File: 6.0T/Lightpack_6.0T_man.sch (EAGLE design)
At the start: 32 parts, among them IC1 AT90USB162, IC2 DM631_SOP24, IC3 DM631_SOP24, J1 DCJ0202, Q1 16Mhz, X1 USB-MICRO-B

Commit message: Front-line I/O rearranged
* Button --> DJK02A --> microUSB
* Expand PCB size for Alex case
* Bottom polygons shape changes
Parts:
- U$1: value RJ11-5P-REEL-LIGHTPACK6T -> RJ11-5P-REEL-LIGHTPACK6T2; device _RJ11:RJ11-5P-REEL-LIGHTPACK6T -> _RJ11:RJ11-5P-REEL-LIGHTPACK6T2
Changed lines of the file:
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@@
 <part name="SV1" library="_brd-conn" deviceset="UART3" device=""/>
 <part name="GND5" library="supply1" deviceset="GND" device=""/>
-<part name="U$1" library="_RJ11" deviceset="RJ11-5P-REEL" device="-LIGHTPACK6T"/>
+<part name="U$1" library="_RJ11" deviceset="RJ11-5P-REEL" device="-LIGHTPACK6T2"/>
 <part name="U$2" library="_RJ11" deviceset="RJ11-5P-REEL" device="-MAIN"/>
 <part name="J1" library="_connectors" deviceset="DCJ0202" device=""/>

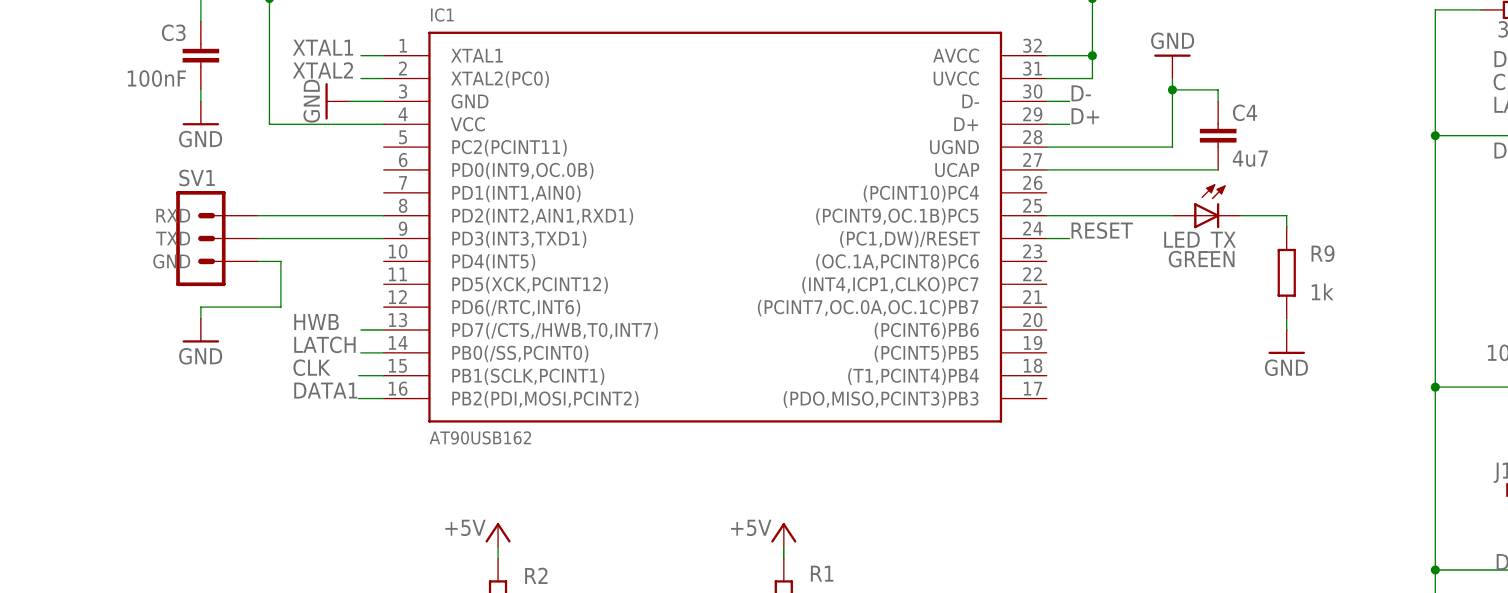
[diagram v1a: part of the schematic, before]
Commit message: 60T improved for casing
* PCB size 76x71mm now
* UART deletted
* ACT LED now on pin 10 instead 25 (need to modify firmware)
* ACT LED thru-hole d3 now (need to test R9)
* 3 mount holes d3 od5
* Significanty alot of space between components
* I/O ports now adjust for Alex case
* Silkscreen info added
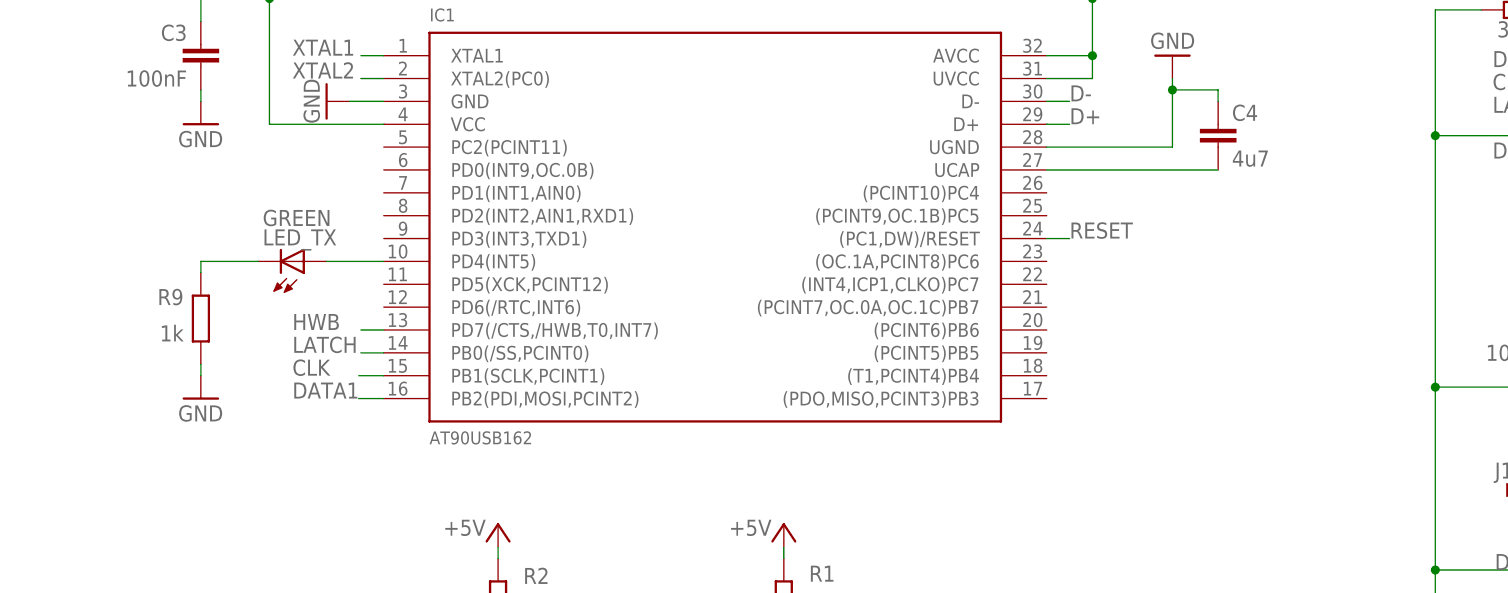
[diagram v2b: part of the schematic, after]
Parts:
- removed SV1: (no value), _brd-conn:UART3
- LED_TX: device led:LEDCHIPLED_0805 -> adafruit:LED3MM
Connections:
- removed net N$4: IC1.PD3(INT3,TXD1), SV1.TXD
- removed net N$8: IC1.(PCINT9,OC.1B)PC5, LED_TX.A
- net GND: no longer SV1.GND
- net N$3: now also IC1.PD4(INT5), LED_TX.A; no longer IC1.PD2(INT2,AIN1,RXD1), SV1.RXD
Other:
- moved on the sheet: LED_TX, R9
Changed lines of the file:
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@@
 <part name="D2" library="diode" deviceset="DIODE-" device="SMB" value="SS14"/>
 <part name="GND9" library="supply1" deviceset="GND" device=""/>
-<part name="LED_TX" library="led" deviceset="LED" device="CHIPLED_0805" value="GREEN"/>
+<part name="LED_TX" library="adafruit" deviceset="LED" device="3MM" value="GREEN"/>
 <part name="GND19" library="supply1" deviceset="GND" device=""/>
 <part name="R9" library="rcl" deviceset="R-EU_" device="R0805" value="1k"/>
@@
 <part name="IC2" library="_LedDrivers" deviceset="DM631" device="_SOP24"/>
 <part name="IC3" library="_LedDrivers" deviceset="DM631" device="_SOP24"/>
-<part name="SV1" library="_brd-conn" deviceset="UART3" device=""/>
-<part name="GND5" library="supply1" deviceset="GND" device=""/>
 <part name="U$1" library="_RJ11" deviceset="RJ11-5P-REEL" device="-LIGHTPACK6T2"/>
 <part name="U$2" library="_RJ11" deviceset="RJ11-5P-REEL" device="-MAIN"/>
@@
 <instance part="D2" gate="G$1" x="232.41" y="167.64"/>
 <instance part="GND9" gate="1" x="66.04" y="123.19"/>
-<instance part="LED_TX" gate="G$1" x="135.89" y="85.09" rot="MR270"/>
-<instance part="GND19" gate="1" x="146.05" y="69.85"/>
-<instance part="R9" gate="G$1" x="146.05" y="78.74" smashed="yes" rot="R90">
-<attribute name="NAME" x="148.59" y="79.9846" size="1.778" layer="95"/>
-<attribute name="VALUE" x="148.59" y="75.692" size="1.778" layer="96"/>
+<instance part="LED_TX" gate="G$1" x="36.83" y="80.01" rot="MR90"/>
+<instance part="GND19" gate="1" x="25.4" y="64.77"/>
+<instance part="R9" gate="G$1" x="25.4" y="73.66" smashed="yes" rot="R90">
+<attribute name="NAME" x="20.574" y="75.1586" size="1.778" layer="95"/>
+<attribute name="VALUE" x="20.828" y="71.12" size="1.778" layer="96"/>
 </instance>
 <instance part="C3" gate="G$1" x="25.4" y="104.14" rot="MR0"/>
@@
 <instance part="IC2" gate="G$1" x="200.66" y="139.7"/>
 <instance part="IC3" gate="G$1" x="200.66" y="86.36"/>
-<instance part="SV1" gate="G$1" x="24.13" y="82.55"/>
-<instance part="GND5" gate="1" x="25.4" y="71.12"/>
 <instance part="U$1" gate="G$1" x="231.14" y="139.7"/>
 <instance part="U$2" gate="G$1" x="231.14" y="86.36"/>
@@
 </segment>
 <segment>
-<wire x1="146.05" y1="73.66" x2="146.05" y2="72.39" width="0.1524" layer="91"/>
+<wire x1="25.4" y1="68.58" x2="25.4" y2="67.31" width="0.1524" layer="91"/>
 <pinref part="GND19" gate="1" pin="GND"/>
 <pinref part="R9" gate="G$1" pin="1"/>
@@
 <pinref part="C7" gate="G$1" pin="-"/>
 <pinref part="GND9" gate="1" pin="GND"/>
-</segment>
-<segment>
-<wire x1="31.75" y1="80.01" x2="34.29" y2="80.01" width="0.1524" layer="91"/>
-<wire x1="34.29" y1="80.01" x2="34.29" y2="74.93" width="0.1524" layer="91"/>
-<wire x1="34.29" y1="74.93" x2="25.4" y2="74.93" width="0.1524" layer="91"/>
-<wire x1="25.4" y1="74.93" x2="25.4" y2="73.66" width="0.1524" layer="91"/>
-<pinref part="SV1" gate="G$1" pin="GND"/>
-<pinref part="GND5" gate="1" pin="GND"/>
 </segment>
 <segment>
@@
 </segment>
 </net>
-<net name="N$8" class="0">
-<segment>
-<wire x1="119.38" y1="85.09" x2="133.35" y2="85.09" width="0.1524" layer="91"/>
-<pinref part="IC1" gate="G$1" pin="(PCINT9,OC.1B)PC5"/>
-<pinref part="LED_TX" gate="G$1" pin="A"/>
-</segment>
-</net>
 <net name="N$37" class="0">
 <segment>
-<wire x1="140.97" y1="85.09" x2="146.05" y2="85.09" width="0.1524" layer="91"/>
-<wire x1="146.05" y1="83.82" x2="146.05" y2="85.09" width="0.1524" layer="91"/>
+<wire x1="25.4" y1="78.74" x2="25.4" y2="80.01" width="0.1524" layer="91"/>
+<pinref part="R9" gate="G$1" pin="2"/>
 <pinref part="LED_TX" gate="G$1" pin="C"/>
-<pinref part="R9" gate="G$1" pin="2"/>
+<wire x1="31.75" y1="80.01" x2="25.4" y2="80.01" width="0.2032" layer="91"/>
 </segment>
 </net>
@@
 </segment>
 </net>
-<net name="N$3" class="0">
-<segment>
-<wire x1="45.72" y1="85.09" x2="31.75" y2="85.09" width="0.1524" layer="91"/>
-<pinref part="IC1" gate="G$1" pin="PD2(INT2,AIN1,RXD1)"/>
-<pinref part="SV1" gate="G$1" pin="RXD"/>
-</segment>
-</net>
-<net name="N$4" class="0">
-<segment>
-<wire x1="45.72" y1="82.55" x2="31.75" y2="82.55" width="0.1524" layer="91"/>
-<pinref part="IC1" gate="G$1" pin="PD3(INT3,TXD1)"/>
-<pinref part="SV1" gate="G$1" pin="TXD"/>
-</segment>
-</net>
 <net name="N$16" class="0">
 <segment>
@@
 </segment>
 </net>
+<net name="N$3" class="0">
+<segment>
+<pinref part="LED_TX" gate="G$1" pin="A"/>
+<pinref part="IC1" gate="G$1" pin="PD4(INT5)"/>
+<wire x1="39.37" y1="80.01" x2="45.72" y2="80.01" width="0.2032" layer="91"/>
+</segment>
+</net>

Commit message: I/O names for tPlace added and rearranged.
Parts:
- removed Q1: 16Mhz, crystal:CRYSTALHC49UP
- added CN1: USB-MICRO-B, _USB_sockets:USB-MICRO-B
- X1: value USB-MICRO-B -> 16Mhz; device _USB_sockets:USB-MICRO-B -> crystal:CRYSTALHC49UP
- renumbered BOOTLOADER to S1, U$1 to CN2, U$2 to CN3
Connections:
- net +5V: now also CN1.VBUS; no longer X1.VBUS
- net GND: now also CN1.GND; no longer X1.GND
- net N$32: now also CN1.D-; no longer X1.D-
- net N$33: now also CN1.D+; no longer X1.D+
- net N$44: now also CN1.SHIELD1; no longer X1.SHIELD1
- net XTAL1: now also X1.1; no longer Q1.1
- net XTAL2: now also X1.2; no longer Q1.2
